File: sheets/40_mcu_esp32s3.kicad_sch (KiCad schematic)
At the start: 0 parts

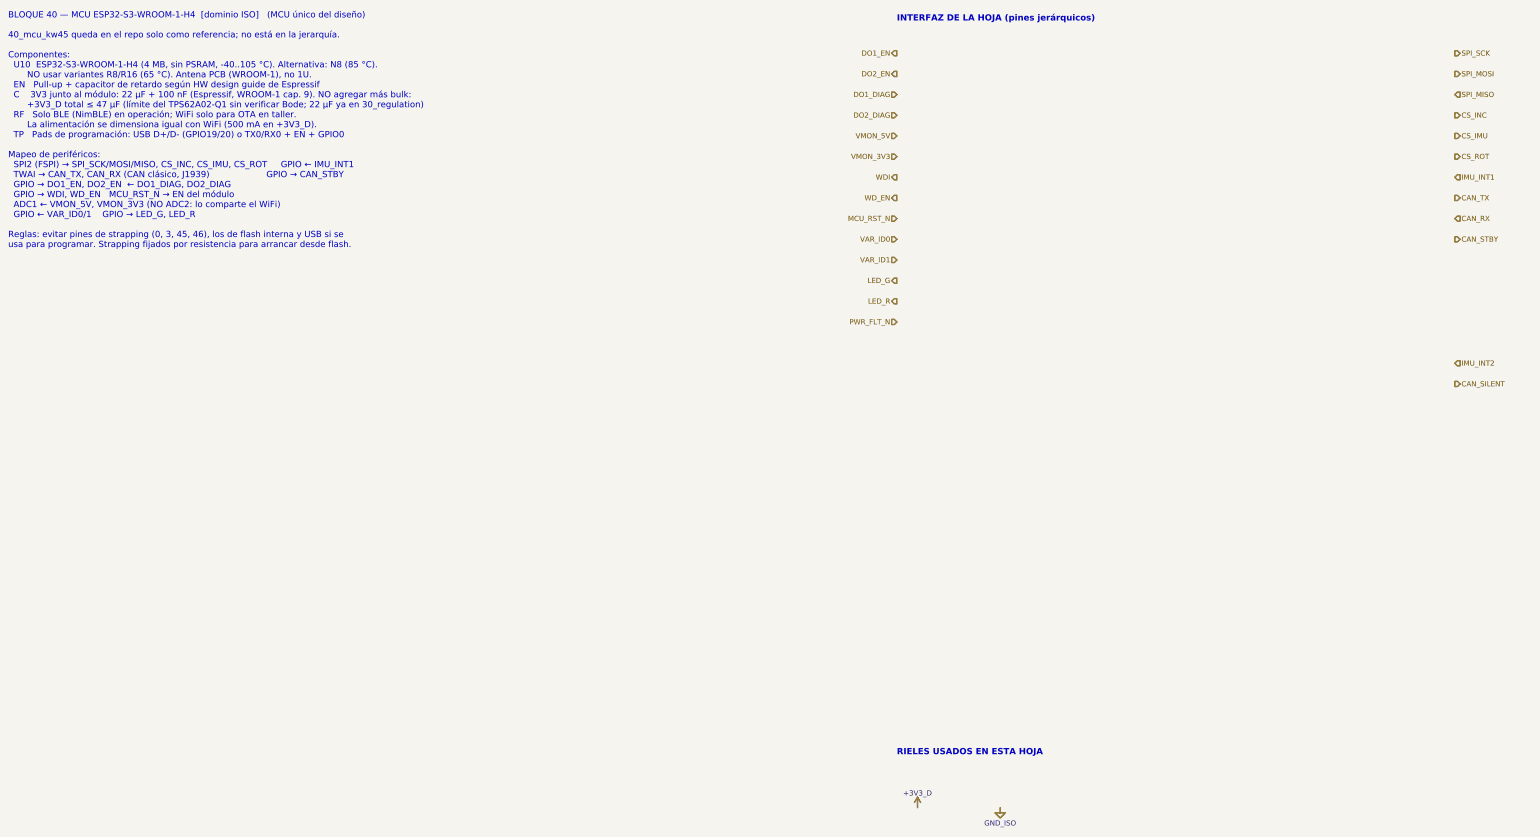
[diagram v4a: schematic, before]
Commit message: [Claude Code] 40_mcu_esp32s3: ESP32-S3-WROOM-1-N8R2, USB-C nativo, UART0 (fase 4)
- U401 ESP32-S3-WROOM-1-N8R2 (símbolo y huella oficiales). Asignación de
  pines aprobada: VMON en ADC1, señales críticas (DO_EN, DIAG, PWR_FLT_N,
  CAN, IMU_INT) en pines sin glitch de encendido, SPI en IO MUX de FSPI,
  strapping/USB/UART0 reservados. Tabla y criterios en la hoja.
- Desacople 22 uF + 100 nF (presupuesto de 47 uF de +3V3_D).
- EN: 10k + 1 uF (Espressif) sobre MCU_RST_N; botones RESET y BOOT.
- USB-C GCT USB4105-GF-A + USBLC6-2SC6 en IO19/20; CC 5.1k; opción de
  banco DNP VBUS -> D401 -> JP401 -> +5V_ISO (~4.6 V, CAN no garantizado).
- Header UART0 (IO43/44), test points de EN, BOOT, VBUS, CAN_TX y CAN_RX.
- Nota de layout de la antena (borde, keepout, orientación respecto al chasis).
- 30_regulation: PWR_FLAG en +3V3_D (la red sale de L301, pasivo).
- ERC 0 en 40 y 30 (100 en el proyecto); sch_visual_qa PASS en ambas.
- docs/PENDIENTES.md: requisitos para 50 (pull-ups de CS a +3V3_A) y 80
  (pull-down en WD_EN), MPN a verificar de la hoja 40.

Co-Authored-By: Claude Opus 5.5 <noreply@anthropic.com>
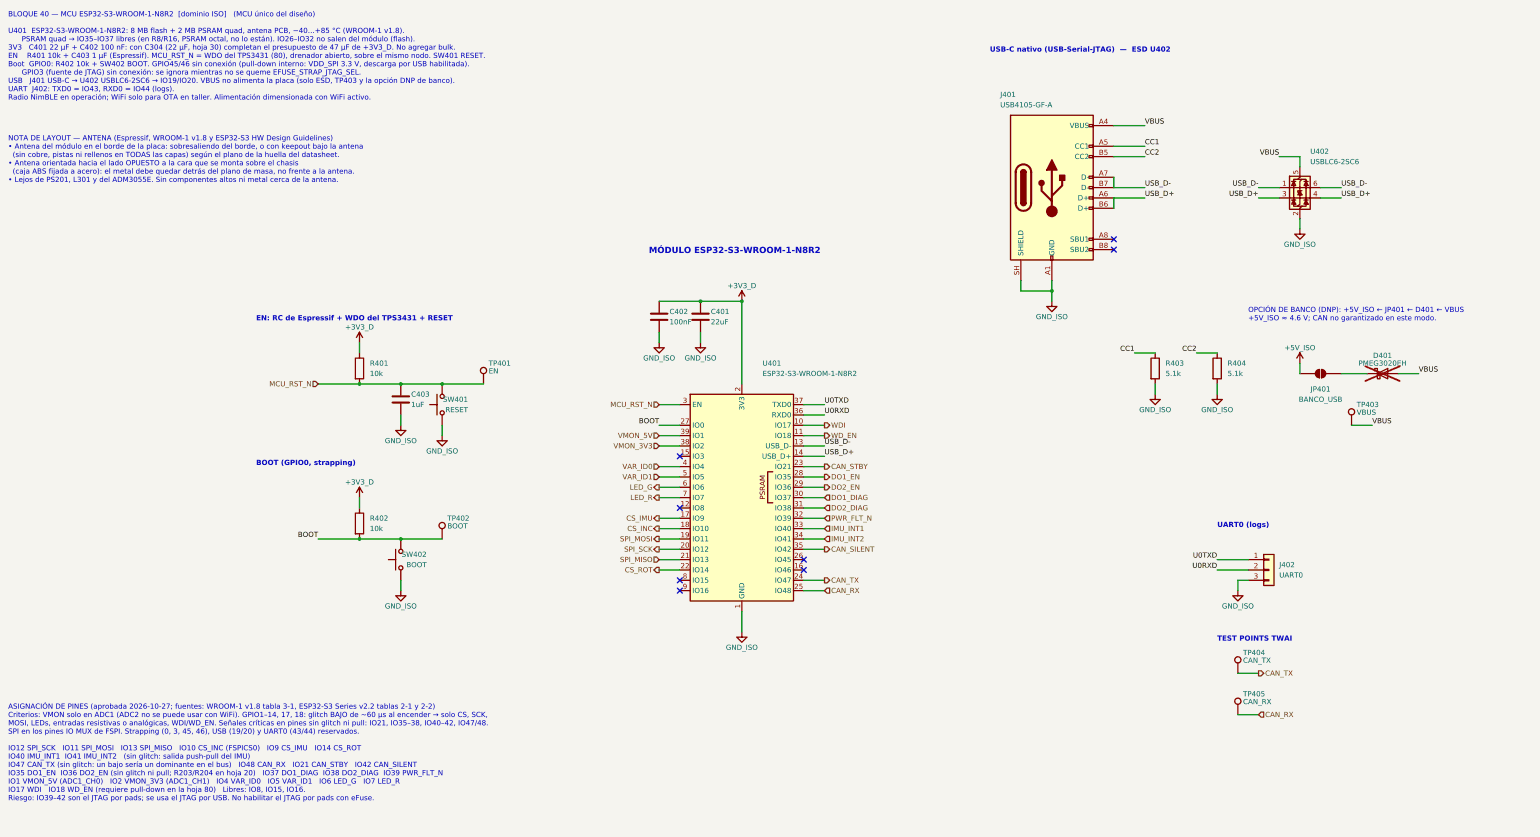
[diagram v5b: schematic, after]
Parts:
- added C401: 22uF, Capacitor_SMD:C_0805_2012Metric, symbol Device:C
- added C402: 100nF, Capacitor_SMD:C_0603_1608Metric, symbol Device:C
- added C403: 1uF, Capacitor_SMD:C_0603_1608Metric, symbol Device:C
- added D401: PMEG3020EH, Diode_SMD:D_SOD-123F, symbol Device:D_Schottky
- added J401: USB4105-GF-A, Connector_USB:USB_C_Receptacle_GCT_USB4105-xx-A_16P_TopMnt_Horizontal, symbol Connector:USB_C_Receptacle_USB2.0_16P
- added J402: UART0, Connector_PinHeader_2.54mm:PinHeader_1x03_P2.54mm_Vertical, symbol Connector_Generic:Conn_01x03
- added JP401: BANCO_USB, Jumper:SolderJumper-2_P1.3mm_Open_RoundedPad1.0x1.5mm, symbol Jumper:SolderJumper_2_Open
- added R401, R402: 10k, Resistor_SMD:R_0603_1608Metric, symbol Device:R
- added R403, R404: 5.1k, Resistor_SMD:R_0603_1608Metric, symbol Device:R
- added SW401: RESET, Button_Switch_THT:SW_PUSH_6mm, symbol Switch:SW_Push
- added SW402: BOOT, Button_Switch_THT:SW_PUSH_6mm, symbol Switch:SW_Push
- added TP401: EN, TestPoint:TestPoint_Pad_D1.5mm, symbol Connector:TestPoint
- added TP402: BOOT, TestPoint:TestPoint_Pad_D1.5mm, symbol Connector:TestPoint
- added TP403: VBUS, TestPoint:TestPoint_Pad_D1.5mm, symbol Connector:TestPoint
- added TP404: CAN_TX, TestPoint:TestPoint_Pad_D1.5mm, symbol Connector:TestPoint
- added TP405: CAN_RX, TestPoint:TestPoint_Pad_D1.5mm, symbol Connector:TestPoint
- added U401: ESP32-S3-WROOM-1-N8R2, RF_Module:ESP32-S3-WROOM-1, symbol RF_Module:ESP32-S3-WROOM-1
- added U402: USBLC6-2SC6, Package_TO_SOT_SMD:SOT-23-6, symbol Power_Protection:USBLC6-2SC6
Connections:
- net +3V3_D: now also C401.1, C402.1, R401.1, R402.1, U401.2 (3V3)
- net CAN_RX: now also TP405.1, U401.25 (IO48)
- net CAN_SILENT: now also U401.35 (IO42)
- net CAN_STBY: now also U401.23 (IO21)
- net CAN_TX: now also TP404.1, U401.24 (IO47)
- net CS_IMU: now also U401.17 (IO9)
- net CS_INC: now also U401.18 (IO10)
- net CS_ROT: now also U401.22 (IO14)
- net DO1_DIAG: now also U401.30 (IO37)
- net DO1_EN: now also U401.28 (IO35)
- net DO2_DIAG: now also U401.31 (IO38)
- net DO2_EN: now also U401.29 (IO36)
- net GND_ISO: now also C401.2, C402.2, C403.2, J401.A1 (GND), J401.A12 (GND), J401.B1 (GND), J401.B12 (GND), J401.SH (SHIELD), J402.3 (Pin_3), R403.2, R404.2, SW401.1, SW402.1, U401.1 (GND), U401.40 (GND), U401.41 (GND), U402.2 (GND)
- net IMU_INT1: now also U401.33 (IO40)
- net IMU_INT2: now also U401.34 (IO41)
- net LED_G: now also U401.6 (IO6)
- net LED_R: now also U401.7 (IO7)
- net MCU_RST_N: now also C403.1, R401.2, SW401.2, TP401.1, U401.3 (EN)
- net PWR_FLT_N: now also U401.32 (IO39)
- net SPI_MISO: now also U401.21 (IO13)
- net SPI_MOSI: now also U401.19 (IO11)
- net SPI_SCK: now also U401.20 (IO12)
- net VAR_ID0: now also U401.4 (IO4)
- net VAR_ID1: now also U401.5 (IO5)
- net VMON_3V3: now also U401.38 (IO2)
- net VMON_5V: now also U401.39 (IO1)
- net WDI: now also U401.10 (IO17)
- net WD_EN: now also U401.11 (IO18)
- new net: D401.1 (K), JP401.2 (B)
- new net +5V_ISO: JP401.1 (A)
- new net BOOT: R402.2, SW402.2, TP402.1, U401.27 (IO0)
- new net CC1: J401.A5 (CC1), R403.1
- new net CC2: J401.B5 (CC2), R404.1
- new net U0RXD: J402.2 (Pin_2), U401.36 (RXD0)
- new net U0TXD: J402.1 (Pin_1), U401.37 (TXD0)
- new net USB_D+: J401.A6 (D+), J401.B6 (D+), U401.14 (USB_D+), U402.3 (I/O2), U402.4 (I/O2)
- new net USB_D-: J401.A7 (D-), J401.B7 (D-), U401.13 (USB_D-), U402.1 (I/O1), U402.6 (I/O1)
- new net VBUS: D401.2 (A), J401.A4 (VBUS), J401.A9 (VBUS), J401.B4 (VBUS), J401.B9 (VBUS), TP403.1, U402.5 (VBUS)
- no-connect marks 0 -> 8
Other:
- note added: "ASIGNACIÓN DE PINES (aprobada 2026-10-27; fuentes: WROOM-1 v1.8 tabla 3-1, ESP32-S3 Series v2.2 tablas 2-1 y 2-2) Criterios: VMON solo en ADC1 (ADC2 no se puede usar con WiFi). GPIO1–14, 17, 18: glitch BAJO de ~60 µs al encender → solo CS, SCK, MOSI, LEDs, entradas resistivas o analógicas, WDI/WD_EN. Señales críticas en pines sin glitch ni pull: IO21, IO35–38, IO40–42, IO47/48. SPI en los pines I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"
- note added: "BLOQUE 40 — MCU ESP32-S3-WROOM-1-N8R2 [dominio ISO] (MCU único del diseño) U401 ESP32-S3-WROOM-1-N8R2: 8 MB flash + 2 MB PSRAM quad, antena PCB, −40…+85 °C (WROOM-1 v1.8). PSRAM quad → IO35–IO37 libres (en R8/R16, PSRAM octal, no lo están). IO26–IO32 no salen del módulo (flash). 3V3 C401 22 µF + C402 100 nF: con C304 (22 µF, hoja 30) completan el presupuesto de 47 µF de +3V3_D. No agregar bulk. E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"
- note added: "BOOT (GPIO0, strapping)"
- note added: "EN: RC de Espressif + WDO del TPS3431 + RESET"
- note added: "MÓDULO ESP32-S3-WROOM-1-N8R2"
- note added: "NOTA DE LAYOUT — ANTENA (Espressif, WROOM-1 v1.8 y ESP32-S3 HW Design Guidelines) • Antena del módulo en el borde de la placa: sobresaliendo del borde, o con keepout bajo la antena (sin cobre, pistas ni rellenos en TODAS las capas) según el plano de la huella del datasheet. • Antena orientada hacia el lado OPUESTO a la cara que se monta sobre el chasis (caja ABS fijada a acero): el metal debe que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"
- note added: "OPCIÓN DE BANCO (DNP): +5V_ISO ← JP401 ← D401 ← VBUS +5V_ISO ≈ 4.6 V; CAN no garantizado en este modo."
- note added: "TEST POINTS TWAI"
- note added: "UART0 (logs)"
- note added: "USB-C nativo (USB-Serial-JTAG) — ESD U402"
- note removed: "BLOQUE 40 — MCU ESP32-S3-WROOM-1-H4 [dominio ISO] (MCU único del diseño) 40_mcu_kw45 queda en el repo solo como referencia; no está en la jerarquía. Componentes: U10 ESP32-S3-WROOM-1-H4 (4 MB, sin PSRAM, -40..105 °C). Alternativa: N8 (85 °C). NO usar variantes R8/R16 (65 °C). Antena PCB (WROOM-1), no 1U. EN Pull-up + capacitor de retardo según HW design guide de Espressif C 3V3 junto al módulo: 2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"
- note removed: "INTERFAZ DE LA HOJA (pines jerárquicos)"
- note removed: "RIELES USADOS EN ESTA HOJA"
- title: MCU ESP32-S3-WROOM-1-H4 -> MCU ESP32-S3-WROOM-1-N8R2
